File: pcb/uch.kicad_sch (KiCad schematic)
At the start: 18 parts

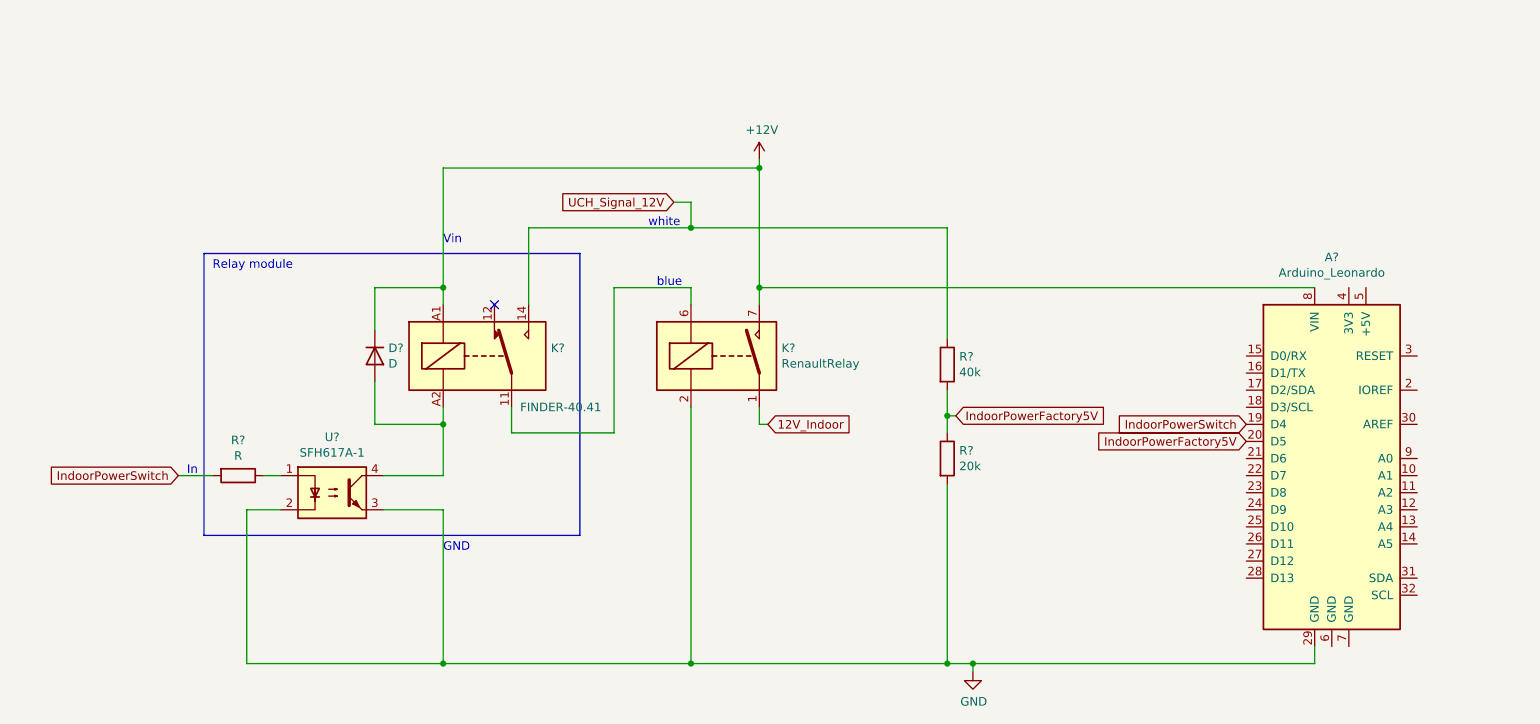
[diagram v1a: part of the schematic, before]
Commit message: `pcb`: deleted the first revision from the schematic
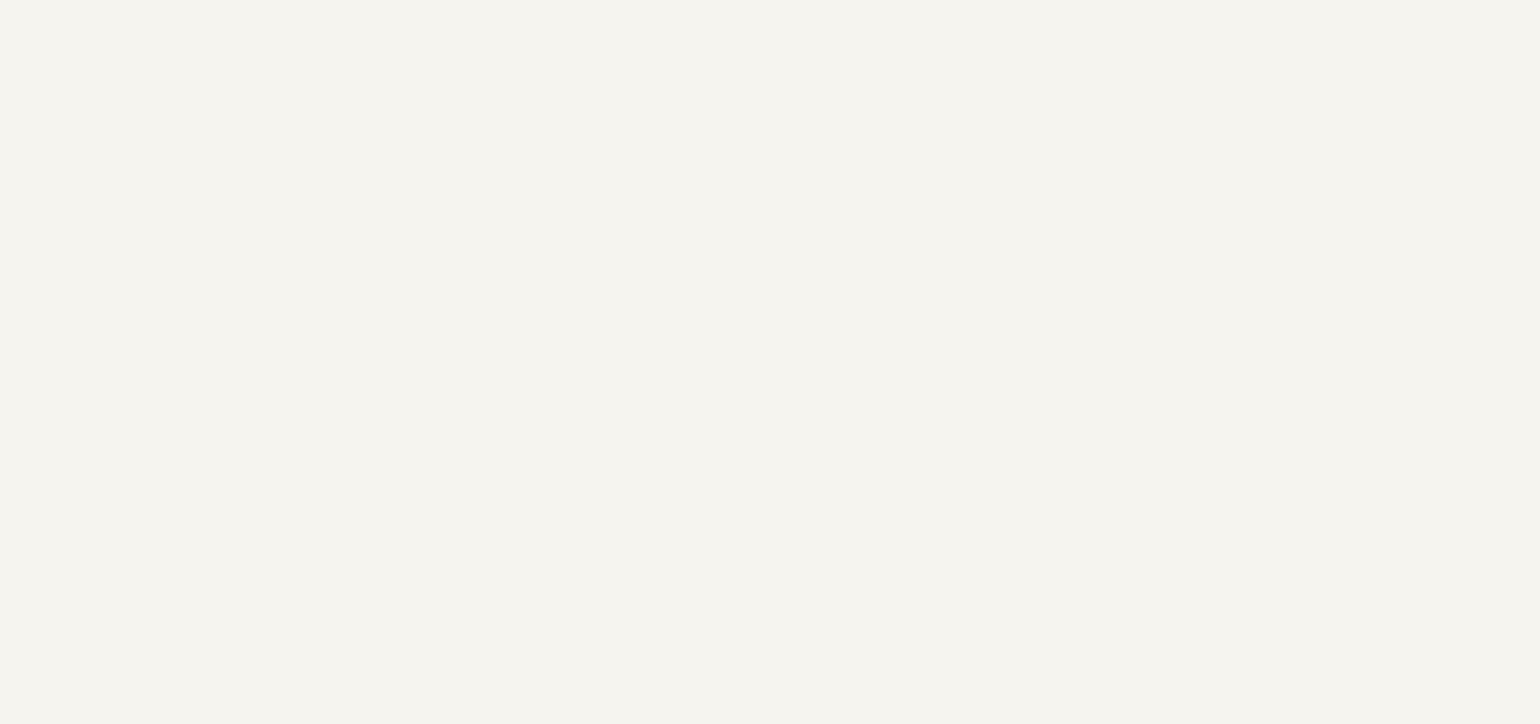
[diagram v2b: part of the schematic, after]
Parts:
- removed A?: Arduino_Leonardo, Module:Arduino_UNO_R3, symbol uch-rescue:Arduino_Leonardo-MCU_Module
- removed D?: D, symbol Device:D
- removed K?: FINDER-40.41, Relay_THT:Relay_SPDT_Finder_40.41, symbol Relay:FINDER-40.41
- removed K?: RenaultRelay, Relay_THT:Relay_StandexMeder_DIP_LowProfile, symbol Relay:DIPxx-1Axx-11x
- removed R?: R, symbol Device:R
- removed R?: 40k, symbol Device:R
- removed R?: 20k, symbol Device:R
- removed U?: SFH617A-1, Package_DIP:DIP-4_W7.62mm, symbol Isolator:SFH617A-1
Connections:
- no-connect marks 18 -> 17
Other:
- note removed: "GND"
- note removed: "In"
- note removed: "Relay module"
- note removed: "Vin"
- note removed: "white"
